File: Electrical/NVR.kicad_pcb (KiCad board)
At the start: 4 copper layers, 120 x 120 mm, 347 parts, among them IC1 RTL8125BG-CG, IC2 ATECC608B-MAHDA-S, IC4 RTL8125BG-CG, J1 Bus_M.2_Socket_M, J10 87427-0442, J11 SS-60300-011, J12 Conn_01x03_Pin, J13 SATA-A-PL-SMT-K, J14 SATA-A-PL-SMT-K, J15 Conn_01x03_Pin, J16 USB_C_Receptacle_USB2.0, J19 SATA-A-PL-SMT-K, J2 SS-60300-011, J20 SATA-A-PL-SMT-K, J21 SATA-A-PL-SMT-K, J22 SATA-A-PL-SMT-K, J3 HDMI_A, J4 USB3_A_Stacked, J5 USB_A_Stacked, J6 Bus_M.2_Socket_E, J7 87427-0442, J8 87427-0442, J9 87427-0442, M1 Fan_4pin, M2 Fan_4pin, Q1 2N7002, Q10 2N7002, Q2 2SK3018, Q3 2SK3018, Q4 2SK3018, Q5 2N7002, Q6 2N7002, Q7 NCE30P28Q, Q8 2N7002, Q9 2N7002, SW1 SW_Push, U1 TPAZ1023-04F, U11 W25Q128JVSIQ, U12 RP2040, U13 HT7533, U14 CH224Q_C46061833, U15 SY8253ADC, U16 SY8253ADC, U2 TPAZ1023-04F, U3 ULC0524P, U4 ULC0524P, U5 ULC0524P, U6 TL431DBZ, U7 SY8253ADC, U79 W25Q128JVSIQ, U8 ASM1166, Y1 25MHz, Y2 25MHz, Y4 25MHz

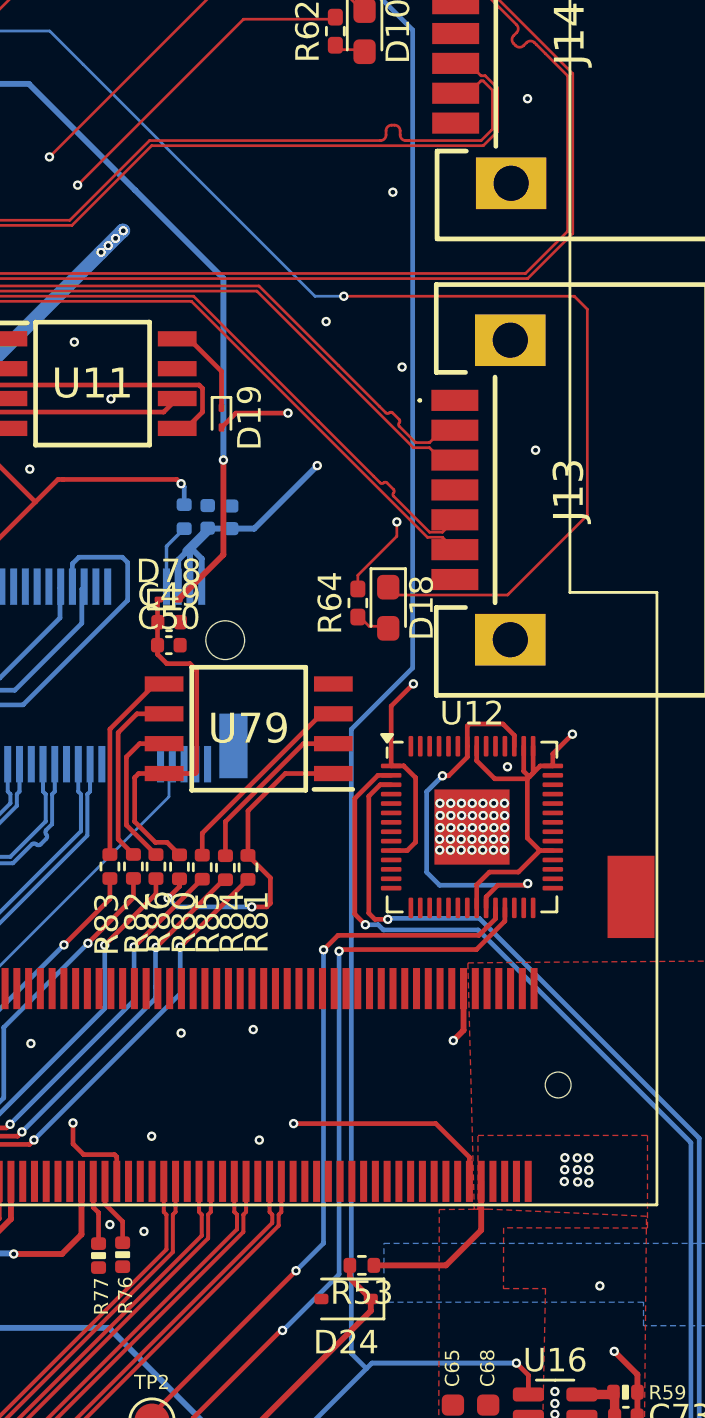
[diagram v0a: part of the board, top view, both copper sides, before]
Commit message: add crystal for rp2040 and update readme
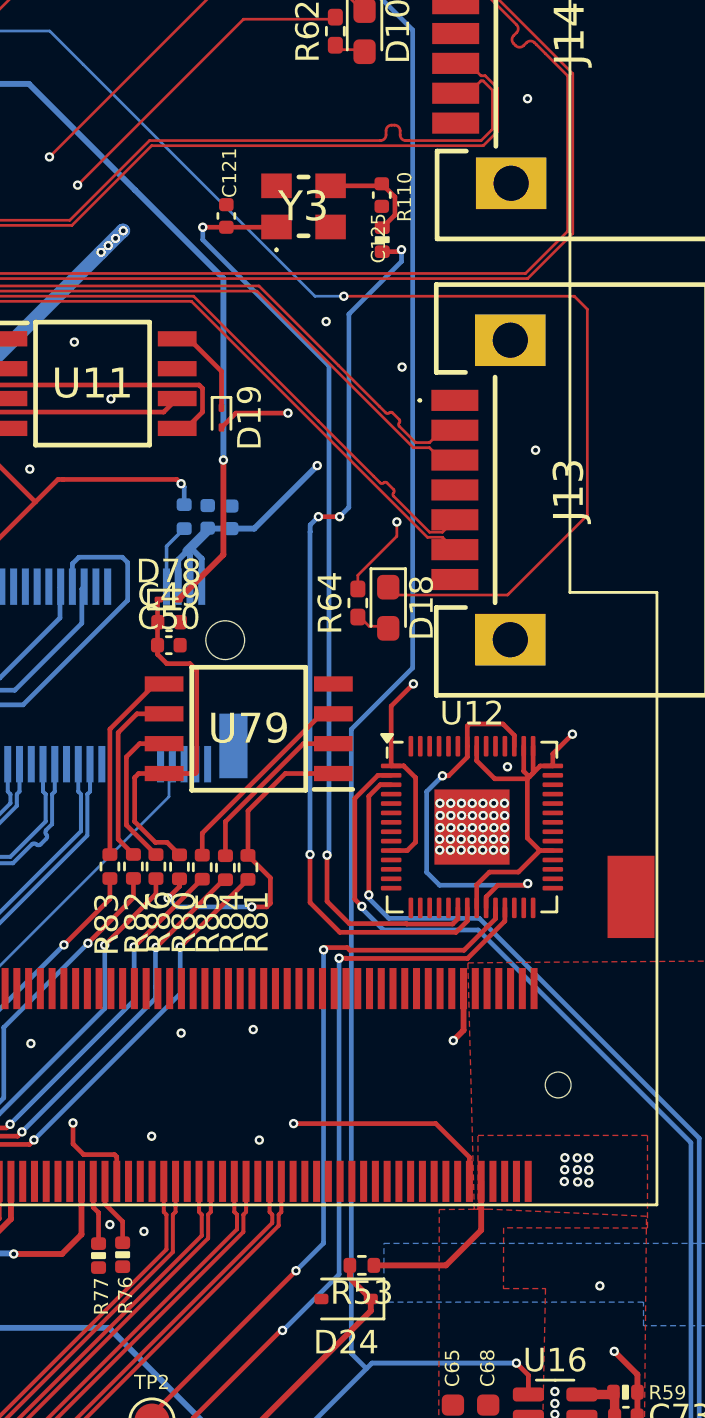
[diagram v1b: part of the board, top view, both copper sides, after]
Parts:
- added C121: 15pF/16V, A_HDJ_Library:C_0402_1005Metric, F.Cu at (317.3, 186.3)
- added C125: 15pF/16V, A_HDJ_Library:C_0402_1005Metric, F.Cu at (323.9, 185.4)
- added R110: 1K/1%, A_HDJ_Library:R_0402_1005Metric, F.Cu at (323.9, 187.3)
- added Y3: ABM8-272-T3, rp crystal:ABM8272T3, F.Cu at (320.6, 185.8)
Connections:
- U12 pad 20: unconnected-(U12-XIN-Pad20) -> Net-(U12-XIN)
- U12 pad 21: unconnected-(U12-XOUT-Pad21) -> Net-(U12-XOUT)
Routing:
- net Net-(U12-XIN): track 0.00 -> 40.6 mm, vias 0 -> 2
- net Net-(U12-XOUT): track 0.00 -> 38.7 mm, vias 0 -> 4
- net Net-(Y3-CRYSTAL_2): track 0.00 -> 4.54 mm
- net GND: vias 696 -> 695
